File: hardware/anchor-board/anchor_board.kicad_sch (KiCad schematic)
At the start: 31 parts, among them U1 DWM3001C, U3 BQ24074, U4 DW01A, U5 FS8205A, U6 TLV75530

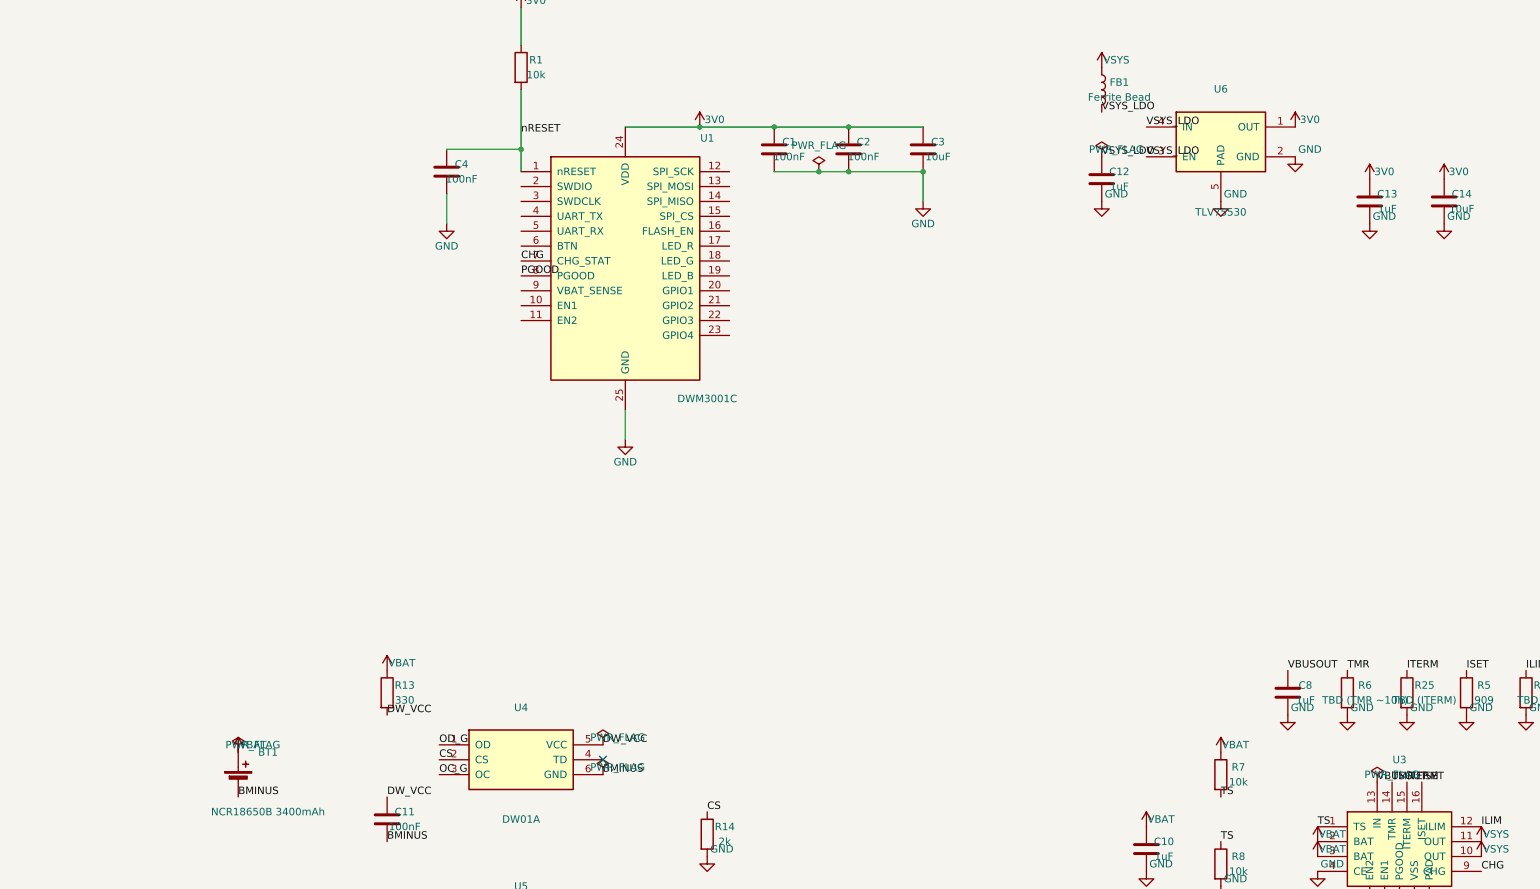
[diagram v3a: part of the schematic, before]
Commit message: hw(anchor-board): capture §4.2 USB-C input + ESD; swap ESD part
- §4.2: J1 USB4105-GF-A + R2/R3 5.1k CC pull-downs, C5 10uF / C6 100nF
  VBUS caps, U2 TPD2E2U06 (CC-line ESD), D2 VBUS TVS, R4 1M + C7 4.7nF
  shield RC. VBUS now connector-driven; data/SBU lines no-connected
  (power-only port).
- Part swap: TPD4S014 -> TPD2E2U06 + dedicated VBUS TVS. The TPD4S014
  is a USB data-port protector, wrong fit for a sink-only power port.
  README §4.2 + bom.md updated to match (+ changelog).
- README §4.3: R24/R25 added for the BQ24074 ILIM/ITERM program pins.
- docs/mcu-tradeoff.md: note JLCPCB's PCBA firmware-flashing service —
  fab can do the one-time bootloader flash, given on-board SWD pads.

ERC: 31 violations - 25 are U1's not-yet-captured §4.6-4.9 / dev-rail
pins, 6 are footprint-not-found for the custom footprints.
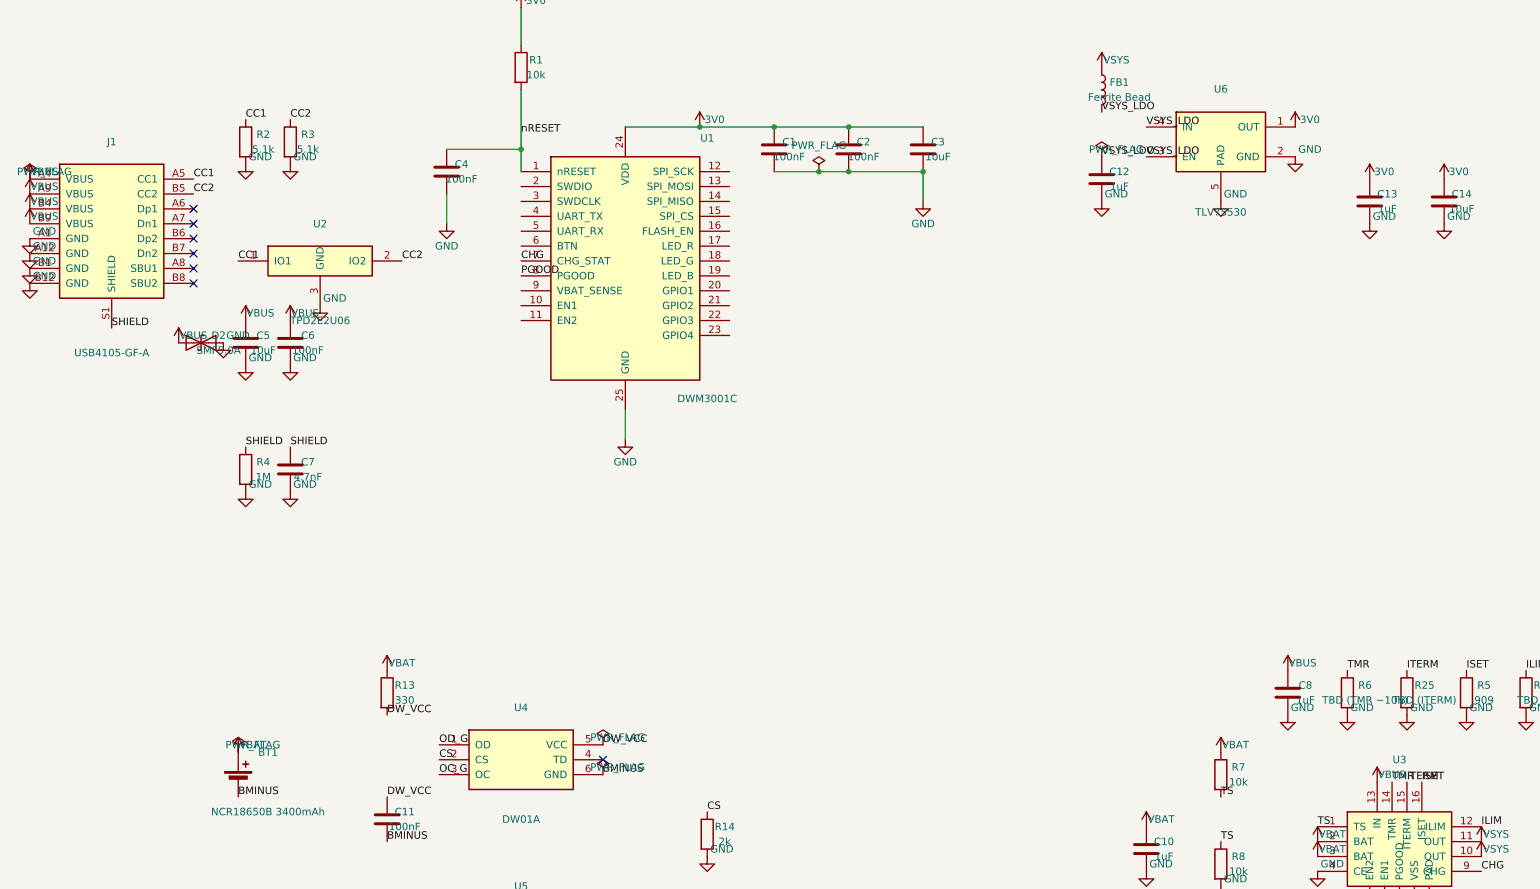
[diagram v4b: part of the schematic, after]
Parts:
- added C5: 10uF, Capacitor_SMD:C_0805_2012Metric, symbol Device:C
- added C6: 100nF, Capacitor_SMD:C_0402_1005Metric, symbol Device:C
- added C7: 4.7nF, Capacitor_SMD:C_0402_1005Metric, symbol Device:C
- added D2: SMF5.0A, Diode_SMD:D_SOD-123, symbol Device:D_TVS
- added J1: USB4105-GF-A, infinity-stumps:USB4105-GF-A, symbol infinity-stumps:USB4105-GF-A
- added R2, R3: 5.1k, Resistor_SMD:R_0402_1005Metric, symbol Device:R
- added R4: 1M, Resistor_SMD:R_0402_1005Metric, symbol Device:R
- added U2: TPD2E2U06, infinity-stumps:TPD2E2U06_SC70, symbol infinity-stumps:TPD2E2U06
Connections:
- net GND: now also C5.2, C6.2, C7.2, D2.2 (A2), J1.A1 (GND), J1.A12 (GND), J1.B1 (GND), J1.B12 (GND), R2.2, R3.2, R4.2, U2.3 (GND)
- net VBUSOUT renamed VBUS
- net VBUS: now also C5.1, C6.1, D2.1 (A1), J1.A4 (VBUS), J1.A9 (VBUS), J1.B4 (VBUS), J1.B9 (VBUS)
- new net CC1: J1.A5 (CC1), R2.1, U2.1 (IO1)
- new net CC2: J1.B5 (CC2), R3.1, U2.2 (IO2)
- new net SHIELD: C7.1, J1.S1 (SHIELD), R4.1
- no-connect marks 1 -> 7

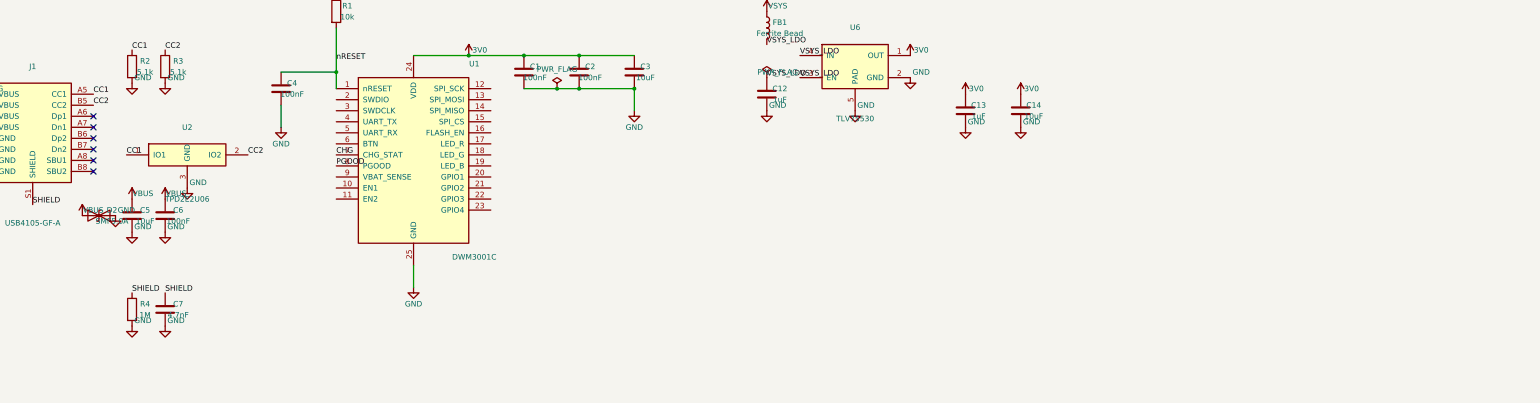
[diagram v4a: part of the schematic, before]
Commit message: hw(anchor-board): capture §4.6 SPI flash + load switch
- §4.6: U7 W25Q128 (16 MB SPI flash) + U8 TPS22916C load switch + C15
  100nF, C16 1uF, R15/R16/R17 10k pull-ups. TPS gates 3V0 -> 3V0_FLASH
  (switched flash rail); SPI bus + FLASH_EN connect to U1, clearing 6
  ERC errors.
- 2 new project symbols: W25Q128JV (SOIC-8), TPS22916C (4-pin WCSP).
- Spec correction: dropped C17 — the TPS22916 has no CT pin (slew rate
  is set by the part variant). README §4.6 + bom.md updated; C16 also
  corrected 0402 -> 0603 for consistency with the other 1uF caps.
- docs/datasheets/: added W25Q128JV + TPS22916 datasheets.

ERC: 26 violations (was 31) - 19 are U1's not-yet-captured §4.7/4.8 /
dev-rail pins, 7 are footprint-not-found for the custom footprints.
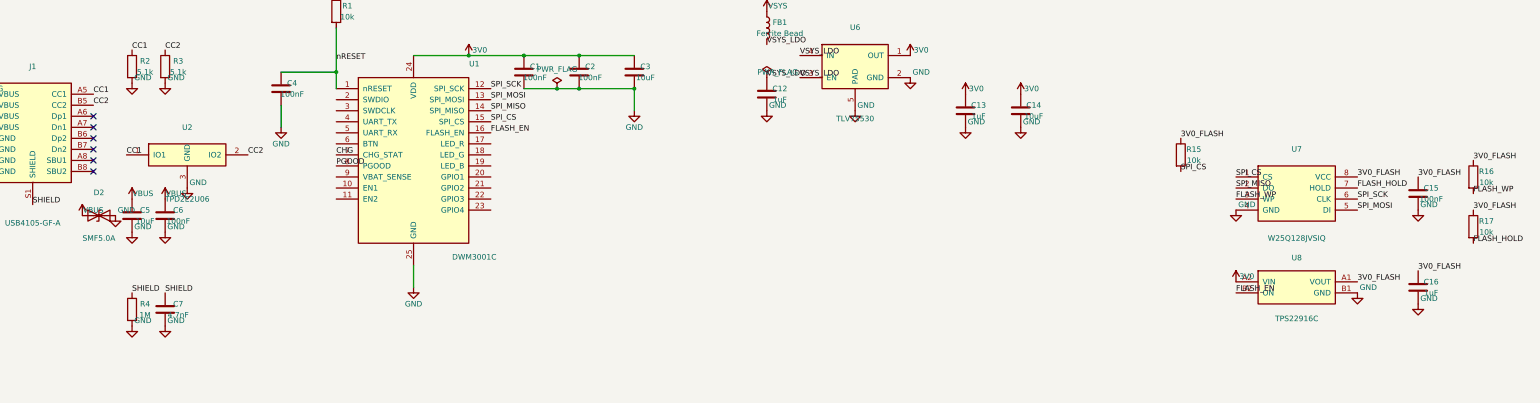
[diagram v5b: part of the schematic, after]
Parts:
- added C15: 100nF, Capacitor_SMD:C_0402_1005Metric, symbol Device:C
- added C16: 1uF, Capacitor_SMD:C_0603_1608Metric, symbol Device:C
- added R15, R16, R17: 10k, Resistor_SMD:R_0402_1005Metric, symbol Device:R
- added U7: W25Q128JVSIQ, Package_SO:SOIC-8_3.9x4.9mm_P1.27mm, symbol infinity-stumps:W25Q128JV
- added U8: TPS22916C, infinity-stumps:TPS22916C_WCSP, symbol infinity-stumps:TPS22916C
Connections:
- net 3V0: now also U8.A2 (VIN)
- net GND: now also C15.2, C16.2, U7.4 (GND), U8.B1 (GND)
- net SPI_SCK: now reaches U1.12 (SPI_SCK)
- net SPI_SCK: now also U7.6 (CLK)
- net SPI_MOSI: now reaches U1.13 (SPI_MOSI)
- net SPI_MOSI: now also U7.5 (DI)
- net SPI_MISO: now reaches U1.14 (SPI_MISO)
- net SPI_MISO: now also U7.2 (DO)
- net SPI_CS: now reaches U1.15 (SPI_CS)
- net SPI_CS: now also R15.2, U7.1 (CS)
- net FLASH_EN: now reaches U1.16 (FLASH_EN)
- net FLASH_EN: now also U8.B2 (ON)
- new net 3V0_FLASH: C15.1, C16.1, R15.1, R16.1, R17.1, U7.8 (VCC), U8.A1 (VOUT)
- new net FLASH_HOLD: R17.2, U7.7 (HOLD)
- new net FLASH_WP: R16.2, U7.3 (WP)

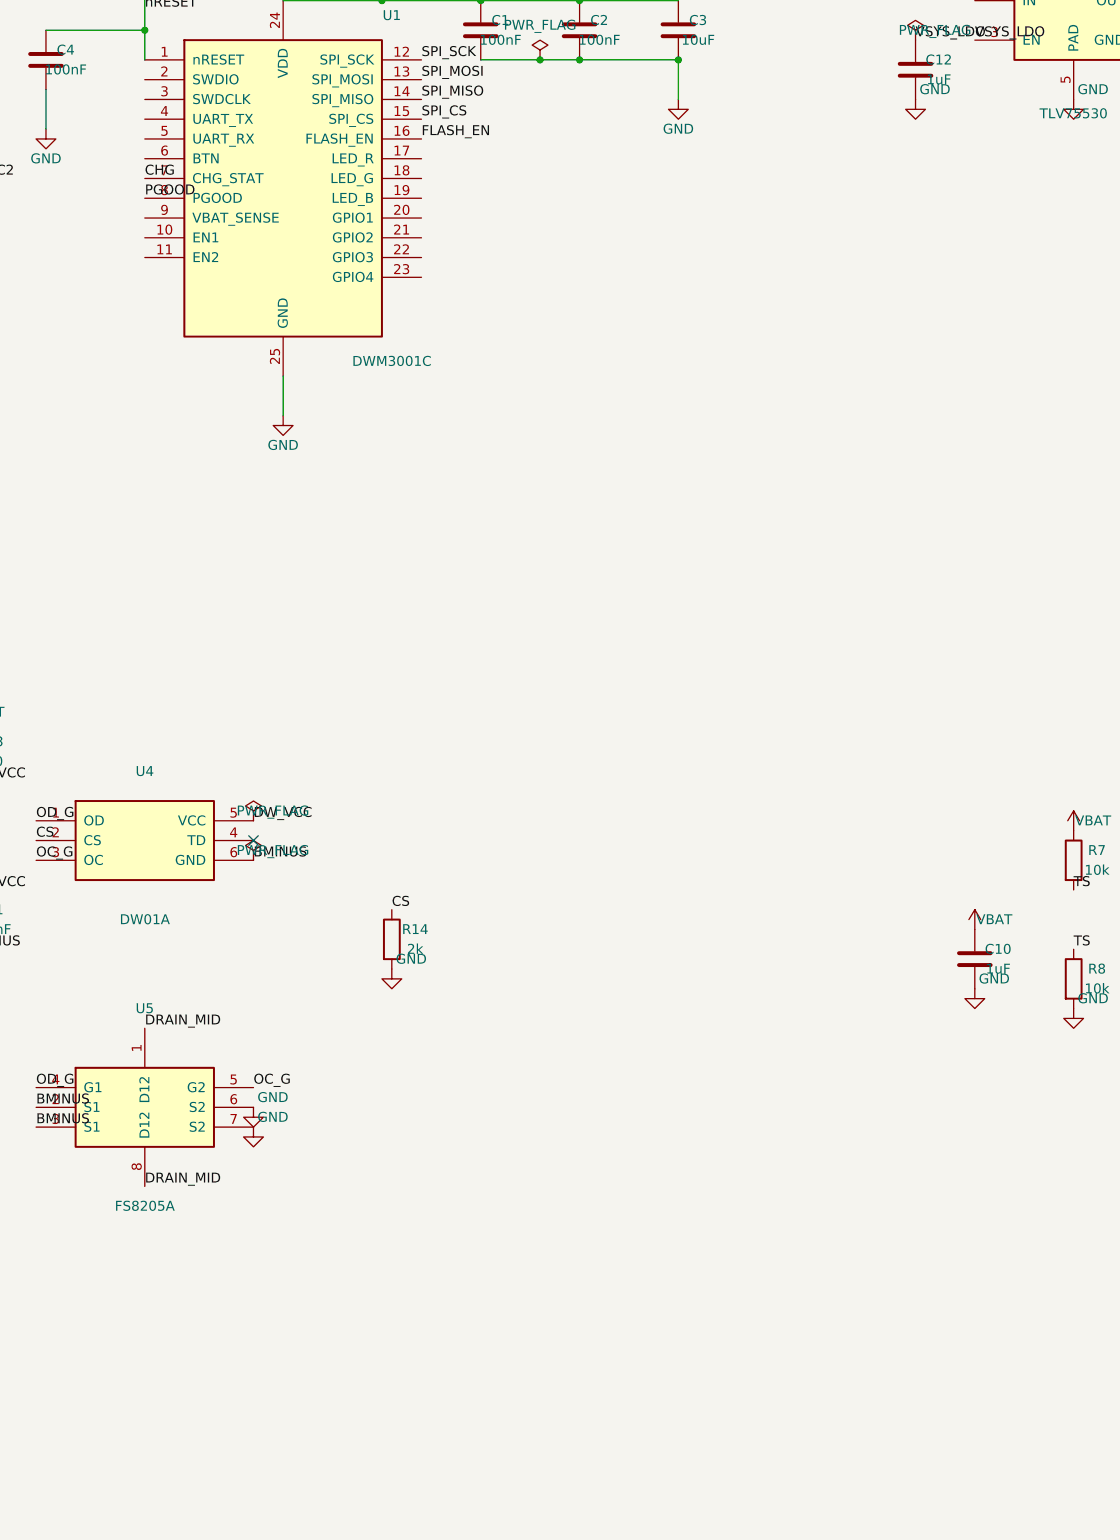
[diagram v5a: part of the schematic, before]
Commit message: Capture §4.7 RGB LED + power button on anchor-board schematic
Adds D1 (common-anode RGB LED) with R18/R19/R20 cathode current-limit
resistors to U1 LED_R/G/B pins, and SW1 power button with R21 pull-up
and C18 debounce cap on the BTN net. U1 EN1/EN2 marked no-connect.
ERC 26 -> 21 (remaining errors are U1 pins captured in §4.8/§4.9).
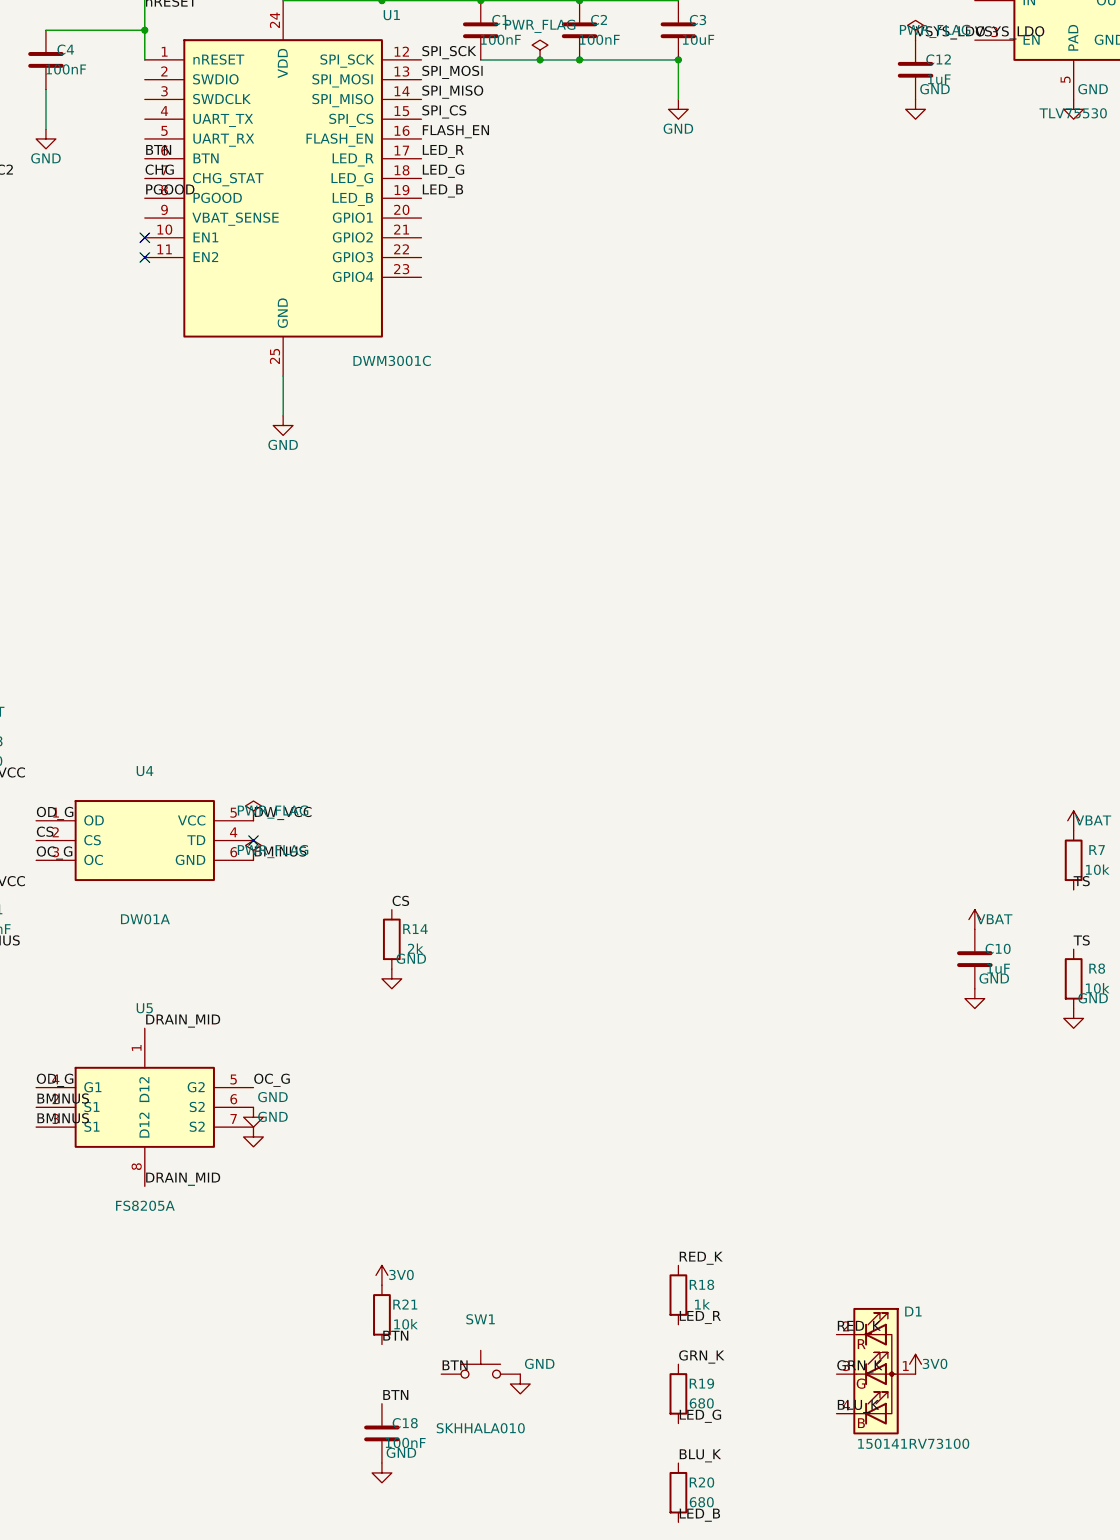
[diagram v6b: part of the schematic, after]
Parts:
- added C18: 100nF, Capacitor_SMD:C_0402_1005Metric, symbol Device:C
- added D1: 150141RV73100, infinity-stumps:LED_RGB_Wurth_150141, symbol Device:LED_ARGB
- added R18: 1k, Resistor_SMD:R_0402_1005Metric, symbol Device:R
- added R19, R20: 680, Resistor_SMD:R_0402_1005Metric, symbol Device:R
- added R21: 10k, Resistor_SMD:R_0402_1005Metric, symbol Device:R
- added SW1: SKHHALA010, infinity-stumps:SW_SKHHALA010, symbol Switch:SW_Push
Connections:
- net 3V0: now also D1.1 (A), R21.1
- net GND: now also C18.2, SW1.2
- net LED_R: now reaches U1.17 (LED_R)
- net LED_R: now also R18.2
- net LED_G: now reaches U1.18 (LED_G)
- net LED_G: now also R19.2
- net LED_B: now reaches U1.19 (LED_B)
- net LED_B: now also R20.2
- net BTN: now reaches U1.6 (BTN)
- net BTN: now also C18.1, R21.2, SW1.1
- new net BLU_K: D1.4 (BK), R20.1
- new net GRN_K: D1.3 (GK), R19.1
- new net RED_K: D1.2 (RK), R18.1
- no-connect marks 7 -> 9
